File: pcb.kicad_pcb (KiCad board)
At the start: 2 copper layers, 60 x 66 mm, 30 parts, among them J2 Conn_01x04_Pin, J3 Conn_01x04_Pin, J4 Conn_01x04_Pin, J5 USB_B_Micro, SW1 SW_SPDT, U1 STM32F103C8Tx, U2 AMS1117-3.3, Y1 16Mhz

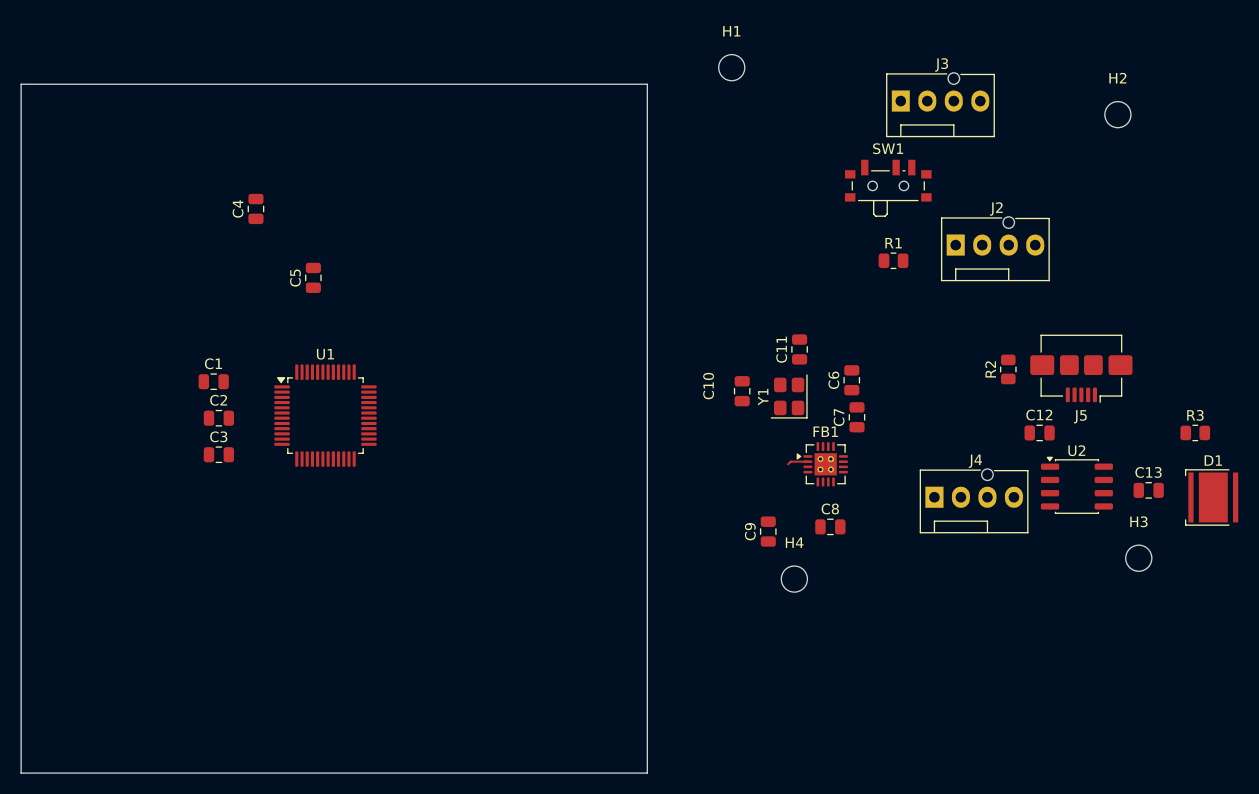
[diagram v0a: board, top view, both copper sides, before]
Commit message: Add STM32 KiCad PCB design
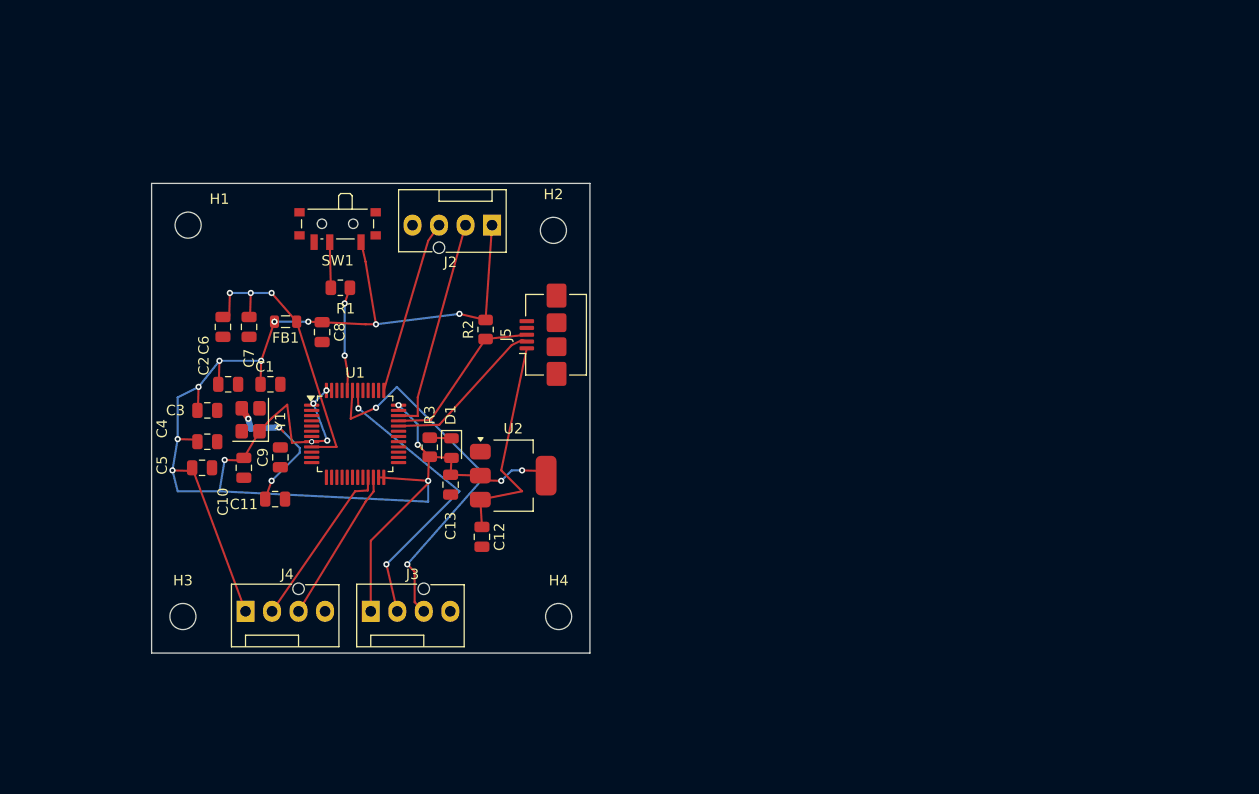
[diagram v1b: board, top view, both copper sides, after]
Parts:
- D1: footprint LED_SMD:LED_Cree-XHP50_3V_HighDensity -> LED_SMD:LED_0805_2012Metric
- FB1: footprint Package_DFN_QFN:Texas_RVA_VQFN-16-1EP_3.5x3.5mm_P0.5mm_EP2.14x2.14mm_ThermalVias -> Inductor_SMD:L_0805_2012Metric
- U2: footprint Package_SO:SO-8_3.9x4.9mm_P1.27mm -> Package_TO_SOT_SMD:SOT-223-3_TabPin2
- moved H3 91.8 mm to (72.5, 93.0)
- moved R3 73.4 mm to (96.2, 76.8), turned to -90 degrees
- moved D1 73.1 mm to (98.2, 76.9), turned to -90 degrees
- moved J3 70.5 mm to (90.5, 92.5)
- moved J4 66.9 mm to (78.5, 92.5)
- moved C13 66.9 mm to (98.2, 80.4), turned to -90 degrees
- moved C6 60.5 mm to (76.3, 65.2), turned to -90 degrees
- moved C7 58.9 mm to (78.8, 65.2), turned to -90 degrees
- moved H2 55.2 mm to (108.0, 56.0)
- moved C12 54.4 mm to (101.2, 85.4), turned to -90 degrees
- moved H1 54.2 mm to (73.0, 55.5)
- moved U2 54.0 mm to (104.2, 79.5)
- moved FB1 53.5 mm to (82.3, 64.8), turned to 180 degrees
- moved R1 53.1 mm to (87.6, 61.5)
- moved SW1 52.9 mm to (87.3, 55.7), turned to 180 degrees
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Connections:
- C1 pad 2: +3.3V -> (no net)
- C10 pad 2: +3.3V -> (no net)
- C11 pad 2: +3.3V -> (no net)
- C12 pad 2: +3.3V -> (no net)
- C13 pad 2: +3.3V -> (no net)
- C2 pad 2: +3.3V -> (no net)
- C3 pad 2: +3.3V -> (no net)
- C4 pad 2: +3.3V -> (no net)
- C5 pad 2: +3.3V -> (no net)
- C6 pad 2: +3.3V -> (no net)
- C7 pad 2: +3.3V -> (no net)
- C8 pad 2: +3.3V -> (no net)
- C9 pad 2: +3.3V -> (no net)
- J2 pad 1: (no net) -> +3.3V
- J2 pad 2: (no net) -> /swdio
- J2 pad 3: (no net) -> /swclk
- J3 pad 1: (no net) -> +3.3V
- J3 pad 3: (no net) -> /URX
- J4 pad 1: (no net) -> +3.3V
- J4 pad 2: (no net) -> /12 scl
- J4 pad 3: +3.3V -> /12 sda
- J5 pad 5: +3.3V -> (no net)
- U1 pad 5: +3.3V -> hsein
- U2 pad 1: +3.3V -> (no net)
- Y1 pad 3: (no net) -> /hse out
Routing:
- net +3.3V: track 2.01 -> 179.7 mm, vias 0 -> 19
- net /URX: track 0.00 -> 36.7 mm, vias 0 -> 2
- net /utx: track 0.00 -> 28.8 mm, vias 0 -> 2
- net +3.3VA: track 0.00 -> 27.1 mm, vias 0 -> 3
- net VBUS: track 0.00 -> 21.5 mm
- net /swdio: track 0.00 -> 20.7 mm
- net /swclk: track 0.00 -> 16.8 mm
- net /12 scl: track 0.00 -> 16.5 mm
- net /usb d+: track 0.00 -> 16.4 mm
- net /usb d-: track 0.00 -> 15.8 mm
- net /12 sda: track 0.00 -> 14.9 mm
- net /hse out: track 0.00 -> 14.4 mm, vias 0 -> 3
- net /BOOTO: track 0.00 -> 9.95 mm, vias 0 -> 2
- net Net-(SW1-B): track 0.00 -> 4.37 mm
- net Net-(D1-K): track 0.00 -> 2.09 mm
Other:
- board size 60 x 66 mm -> 42 x 45 mm
